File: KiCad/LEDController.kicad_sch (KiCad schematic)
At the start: 42 parts, among them SW1 BOOT, SW2 EN, U1 TPS54202DDC, U2 ESP32-S3-WROOM-2, U3 TPS54202DDC

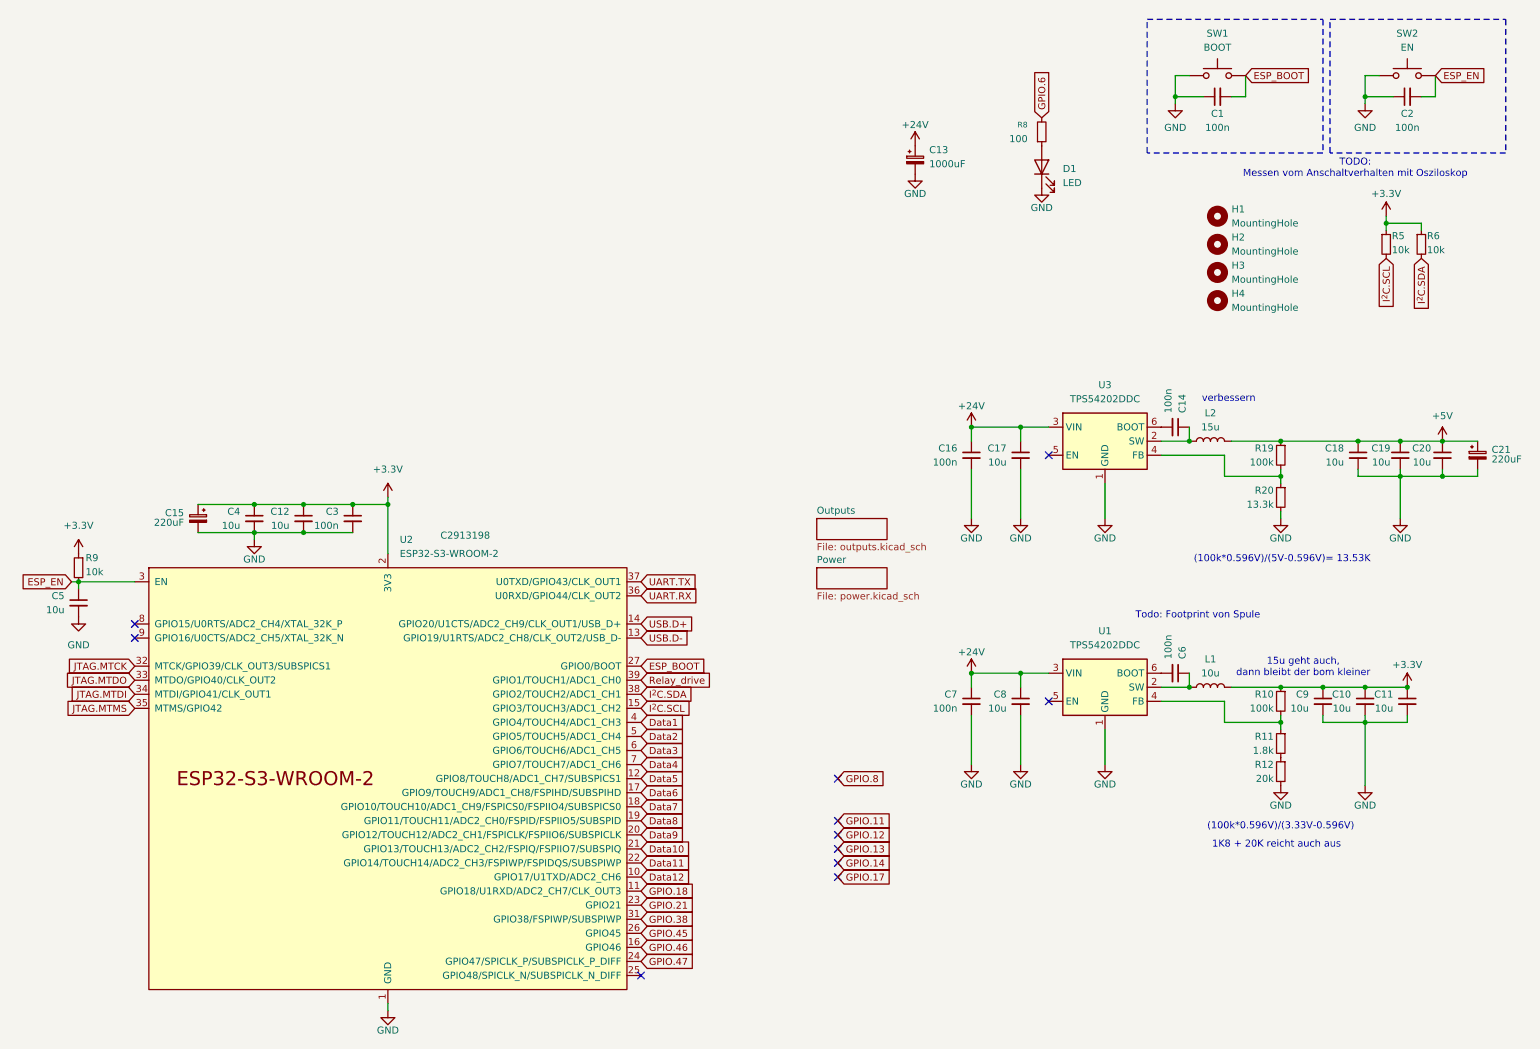
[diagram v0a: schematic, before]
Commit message: add esd protection, pullup on EN, Replicate layout
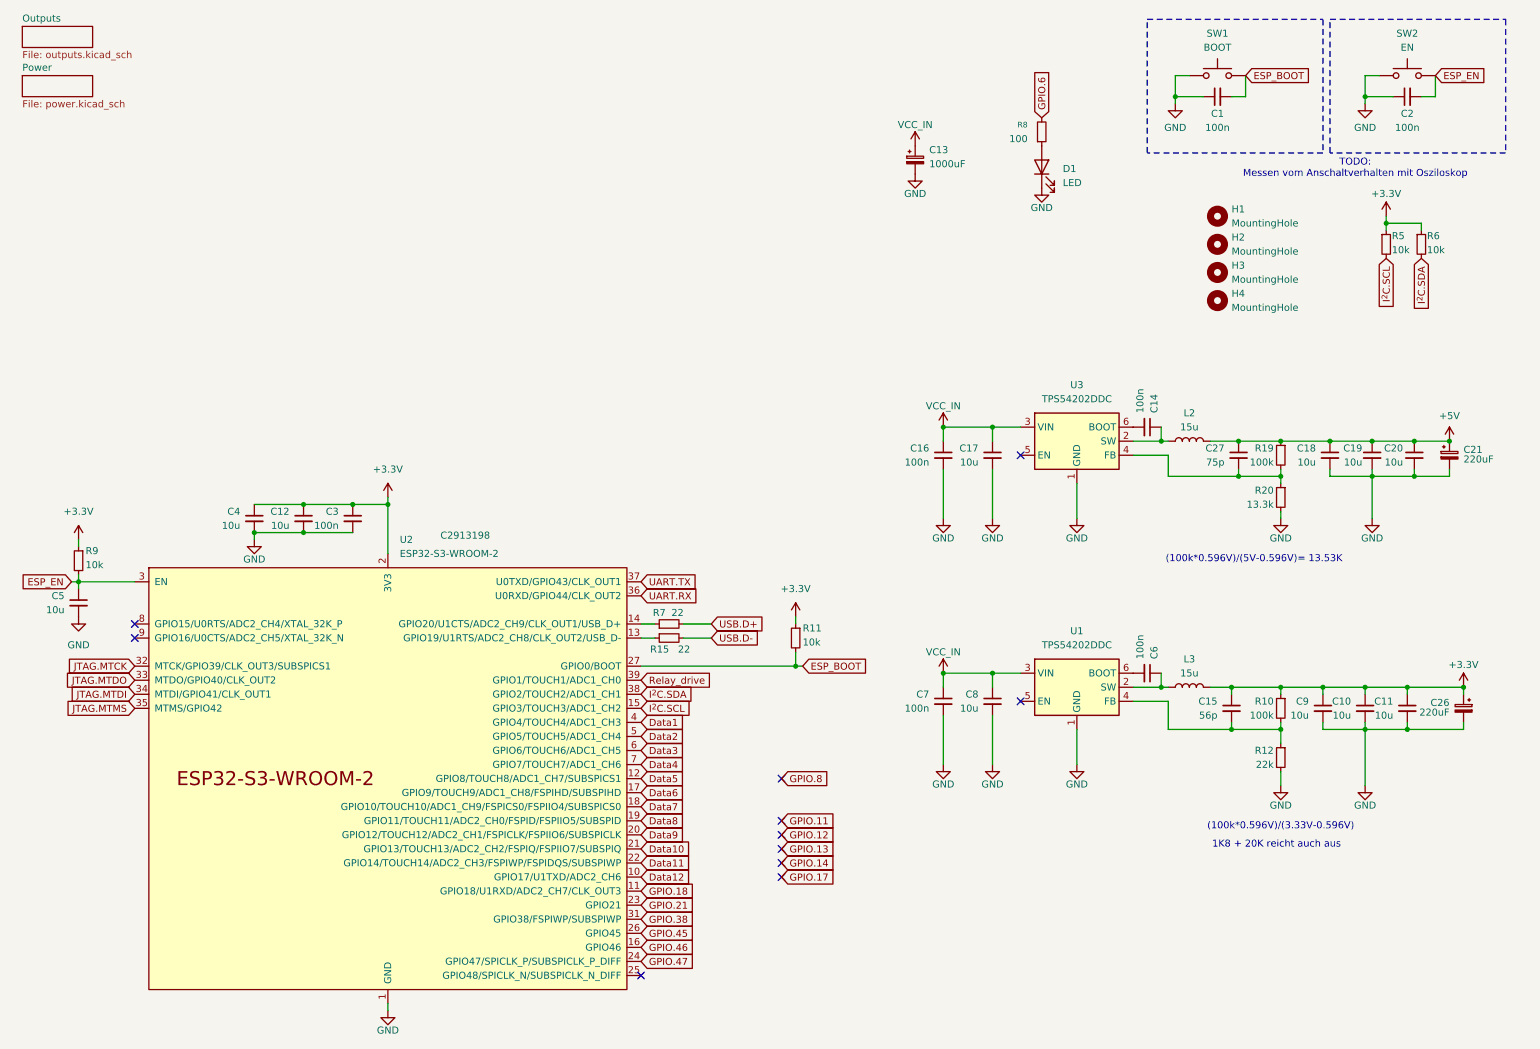
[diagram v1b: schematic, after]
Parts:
- removed C15: 220uF, Capacitor_THT:CP_Radial_D8.0mm_P3.50mm, symbol Device:C_Polarized_Small
- removed L1: 10u, Inductor_SMD:L_APV_ANR4026, symbol Device:L
- added C15: 56p, Capacitor_SMD:C_0805_2012Metric_Pad1.18x1.45mm_HandSolder, symbol Device:C_Small
- added C26: 220uF, Capacitor_THT:CP_Radial_D8.0mm_P3.50mm, symbol Device:C_Polarized_Small
- added C27: 75p, Capacitor_SMD:C_0805_2012Metric_Pad1.18x1.45mm_HandSolder, symbol Device:C_Small
- added L3: 15u, Inductor_SMD:L_APV_APH0630, symbol Device:L
- added R15, R7: 22, Resistor_SMD:R_0805_2012Metric_Pad1.20x1.40mm_HandSolder, symbol Device:R_Small
- L2: footprint Inductor_SMD:L_APV_APH0420 -> Inductor_SMD:L_APV_APH0630; LCSC C5349663 -> C5349699
- R11: value 1.8k -> 10k; LCSC C3017875 -> C2930231
- R12: value 20k -> 22k; LCSC C3017875 -> C2907015
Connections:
- net +3.3V: now also R11.1, C15.1, C26.1, L3.2
- net +5V: now also C27.1
- net ESP_BOOT: now also R11.2
- net GND: now also C26.2
- net USB.D+: now also R7.2; no longer U2.14 (GPIO20/U1CTS/ADC2_CH9/CLK_OUT1/USB_D+)
- net USB.D-: now also R15.2; no longer U2.13 (GPIO19/U1RTS/ADC2_CH8/CLK_OUT2/USB_D-)
- net at R12.1: now also R10.2, U1.4 (FB), C15.2; no longer R11.2
- net at C6.1, U1.2 (SW): now also L3.1
- net at R19.2, R20.1, U3.4 (FB): now also C27.2
- net +24V renamed VCC_IN
- new net: R7.1, U2.14 (GPIO20/U1CTS/ADC2_CH9/CLK_OUT1/USB_D+)
- new net: R15.1, U2.13 (GPIO19/U1RTS/ADC2_CH8/CLK_OUT2/USB_D-)
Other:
- note removed: "15u geht auch, dann bleibt der bom kleiner"
- note removed: "Todo: Footprint von Spule"
- note removed: "verbessern"
- moved on the sheet: C10, C11, C14, C16, C17, C18, C19, C20, C21, C6, C7, C8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

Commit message: prepare tvs diodes
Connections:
- net GPIO.6 is gone; now on net GPIO.18: R8.2
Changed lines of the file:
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@@
-		)
-	)
-	(global_label "GPIO.6"
-		(shape input)
-		(at 198.12 31.75 90)
-		(fields_autoplaced yes)
-		(effects
-			(font
-				(size 1.27 1.27)
-			)
-			(justify left)
-		)
-		(property "Intersheetrefs" "${INTERSHEET_REFS}"
-			(at 198.12 22.4752 90)
-			(hide yes)
-			(show_name no)
-			(do_not_autoplace no)
-			(effects
-				(font
-					(size 1.27 1.27)
-				)
-				(justify left)
-			)
 		)
 	)
@@
 			(hide yes)
 			(show_name no)
+			(do_not_autoplace no)
+			(effects
+				(font
+					(size 1.27 1.27)
+				)
+				(justify left)
+			)
+		)
+	)
+	(global_label "GPIO.18"
+		(shape input)
+		(at 198.12 31.75 90)
+		(fields_autoplaced yes)
+		(effects
+			(font
+				(size 1.27 1.27)
+			)
+			(justify left)
+		)
+		(property "Intersheetrefs" "${INTERSHEET_REFS}"
+			(at 198.12 21.2657 90)
+			(hide yes)
+			(show_name no)

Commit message: add valve driver
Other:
- note added: "komponente neu raussuchen"
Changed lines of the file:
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@@
+		)
+	)
+	(text "komponente neu raussuchen"
+		(exclude_from_sim no)
+		(at 257.81 100.838 0)
+		(effects
+			(font
+				(size 1.27 1.27)
+			)
 		)
 	)

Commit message: .
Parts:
- removed C13: 1000uF, symbol Device:C_Polarized_Small
